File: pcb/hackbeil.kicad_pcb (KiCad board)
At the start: 2 copper layers, 138 x 114 mm, 98 parts

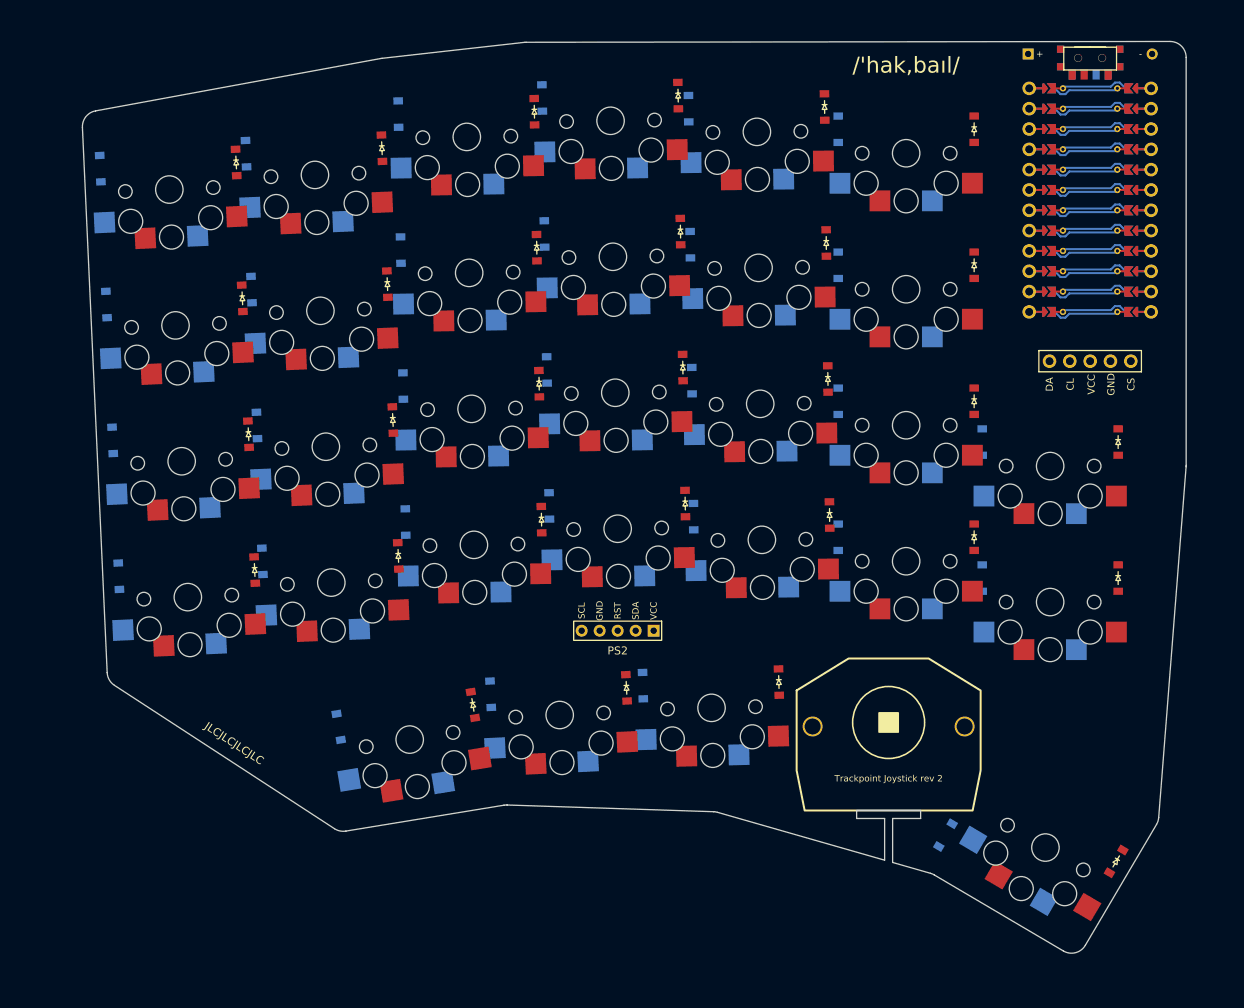
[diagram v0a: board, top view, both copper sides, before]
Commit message: Hand routed PCB
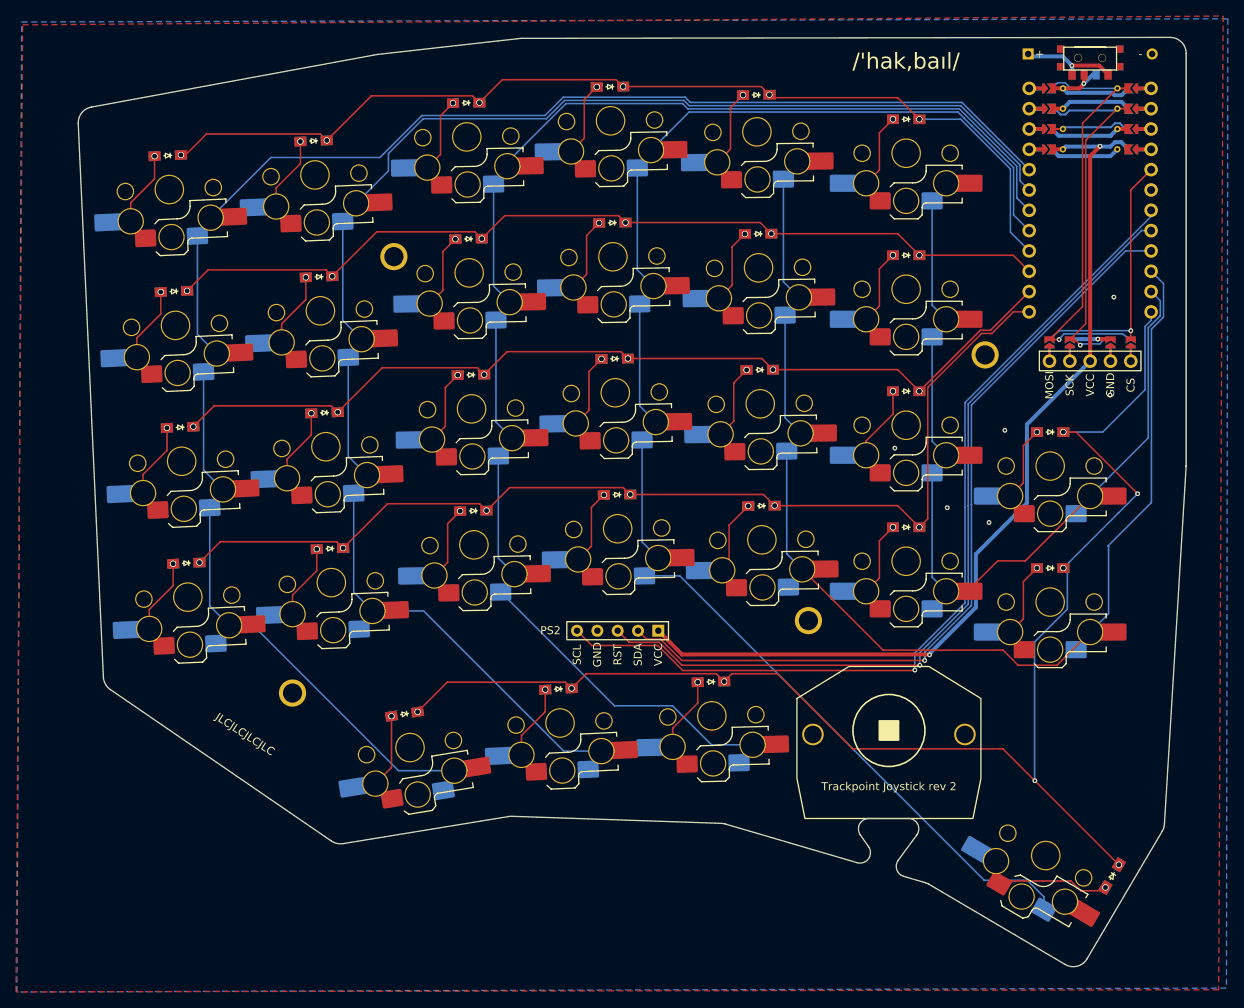
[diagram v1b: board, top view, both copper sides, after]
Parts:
- removed the ? at (219.8, 63.5)
- removed the ? at (135.8, 148.3)
- removed D31, D32, D33, D34, D35, D36, D37, D38, D39, D40, D41, D42, D43, D44, D45, D46, D47, D48, D49, D50, D51, D52, D53, D54, D55, D56, D57, D58, D59, D60: , lib:smd_diode
- added ?: , lib:text, F.Cu at (137.2, 147.1)
- added ?: , lib:text, F.Cu at (219.8, 63.0)
- added MH1: , ceoloide:mounting_hole_npth, F.Cu at (143.1, 142.0)
- added MH2: , ceoloide:mounting_hole_npth, F.Cu at (155.8, 87.4)
- added MH3: , ceoloide:mounting_hole_npth, F.Cu at (207.6, 132.9)
- added MH4: , ceoloide:mounting_hole_npth, F.Cu at (229.7, 99.7)
- S1, S10, S11, S12, S13, S14, S15, S16, S17, S18, S19, S2, S20, S21, S22, S23, S24, S25, S26, S27, S28, S29, S3, S30, S4, S5, S6, S7, S8, S9: footprint PG1350 -> ceoloide:switch_choc_v1_v2; moved to B.Cu
- moved D20 8.68 mm to (201.1, 67.2), turned to -179.3 degrees
- moved D27 8.63 mm to (157.1, 144.6), turned to -170.7 degrees
- moved D1 8.59 mm to (129.8, 125.8), turned to -177.4 degrees
- moved D5 8.59 mm to (147.8, 123.9), turned to -177.7 degrees
- moved D16 8.59 mm to (182.8, 66.2), turned to -179 degrees
- moved D7 8.59 mm to (146.4, 90.0), turned to -177.7 degrees
- moved D21 8.59 mm to (219.8, 121.3), turned to 180 degrees
- moved D22 8.59 mm to (219.8, 104.3), turned to 180 degrees
- moved D23 8.59 mm to (219.8, 87.3), turned to 180 degrees
- moved D24 8.59 mm to (219.8, 70.3), turned to 180 degrees
- moved D15 8.59 mm to (183.1, 83.2), turned to -179 degrees
- moved D25 8.59 mm to (237.8, 126.4), turned to 180 degrees
- moved D26 8.59 mm to (237.8, 109.4), turned to 180 degrees
- moved D14 8.59 mm to (183.4, 100.2), turned to -179 degrees
- moved D17 8.59 mm to (201.7, 118.6), turned to -179.3 degrees
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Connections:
- ? pad 2: P08 -> TP_SDA
- ? pad 3: P08 -> TP_RST
- ? pad 5: P06 -> TP_SCL
- DISP1 pad 1: P10 -> DISP1_1
- DISP1 pad 2: GND -> VCC
- DISP1 pad 3: VCC -> DISP1_3
- DISP1 pad 4: P3 -> DISP1_4
- DISP1 pad 5: P2 -> DISP1_0
- MCU1 pad 10: MCU1_10 -> COL4
- MCU1 pad 101: P1 -> NV_MOSI
- MCU1 pad 102: P0 -> NV_SCK
- MCU1 pad 11: MCU1_11 -> COL5
- MCU1 pad 12: MCU1_12 -> ROW4
- MCU1 pad 13: MCU1_13 -> ROW3
- MCU1 pad 14: MCU1_14 -> ROW2
- MCU1 pad 15: MCU1_15 -> ROW1
- MCU1 pad 16: MCU1_16 -> ROW0
- MCU1 pad 17: MCU1_17 -> COL3
- MCU1 pad 18: MCU1_18 -> COL2
- MCU1 pad 19: MCU1_19 -> COL1
- MCU1 pad 20: MCU1_20 -> COL0
- MCU1 pad 5: MCU1_5 -> NV_CS
- MCU1 pad 6: MCU1_6 -> (no net)
- MCU1 pad 7: MCU1_7 -> TP_SCL
- MCU1 pad 8: MCU1_8 -> TP_RST
- MCU1 pad 9: MCU1_9 -> TP_SDA
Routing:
- net (no net): track 337.7 -> 0.00 mm
- net COL0: track 0.00 -> 196.6 mm
- net ROW4: track 0.00 -> 179.6 mm, vias 0 -> 8
- net COL1: track 0.00 -> 179.5 mm
- net COL3: track 0.00 -> 173.8 mm
- net COL2: track 0.00 -> 163.8 mm
- net COL4: track 0.00 -> 139.0 mm
- net ROW3: track 0.00 -> 131.8 mm, vias 0 -> 6
- net ROW0: track 0.00 -> 124.8 mm, vias 0 -> 6
- net VCC: track 0.00 -> 118.2 mm, vias 0 -> 2
- net ROW2: track 0.00 -> 117.0 mm, vias 0 -> 6
- net TP_SCL: track 0.00 -> 114.0 mm, vias 0 -> 1
- net ROW1: track 0.00 -> 113.4 mm, vias 0 -> 6
- net TP_RST: track 0.00 -> 106.6 mm, vias 0 -> 1
- net TP_SDA: track 0.00 -> 102.2 mm, vias 0 -> 1
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- added copper zone on B.Cu, net GND
- added copper zone on F.Cu, net GND
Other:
- board size 138 x 114 mm -> 138.5 x 116.2 mm

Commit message: Add teardrops and smooth traces
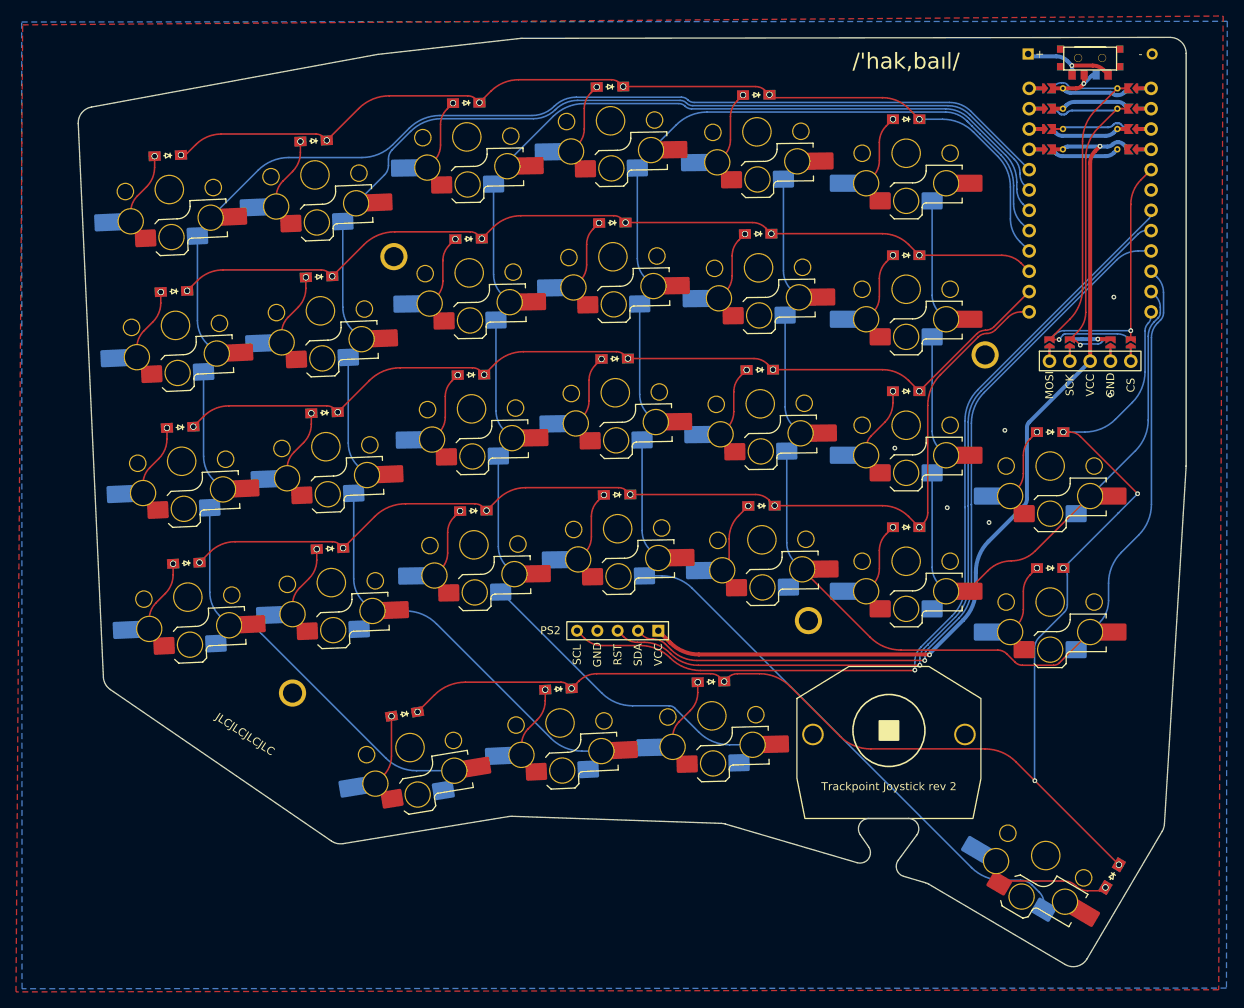
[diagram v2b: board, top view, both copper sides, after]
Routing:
- net COL0: track 196.6 -> 193.1 mm
- net COL1: track 179.5 -> 176.9 mm
- net COL2: track 163.8 -> 161.3 mm
- net ROW4: track 179.6 -> 177.3 mm
- net COL3: track 173.8 -> 171.7 mm
- net COL4: track 139.0 -> 137.0 mm
- net ROW0: track 124.8 -> 122.8 mm
- net ROW3: track 131.8 -> 129.9 mm
- net ROW1: track 113.4 -> 112.0 mm
- net ROW2: track 117.0 -> 115.6 mm
- net TP_SCL: track 114.0 -> 112.7 mm
- net COL5: track 96.5 -> 95.2 mm
- net VCC: track 118.2 -> 116.9 mm
- net TP_RST: track 106.6 -> 105.5 mm
- net TP_SDA: track 102.2 -> 101.0 mm
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
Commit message: Traced by combination of freerouting and manual routing
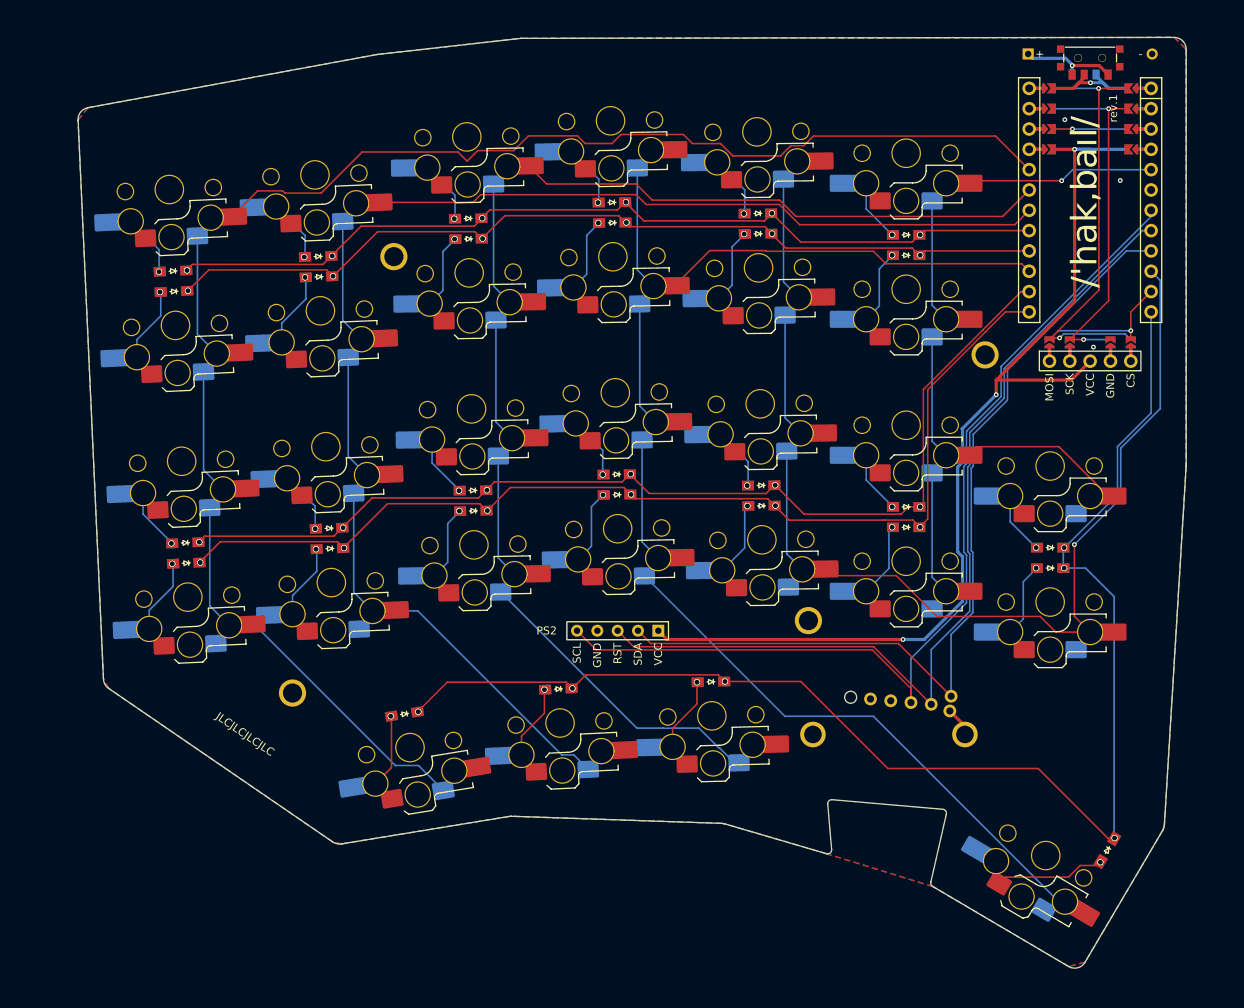
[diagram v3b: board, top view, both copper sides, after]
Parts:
- removed ?: , lib:trackpoint_header
- removed ?: , lib:niceview_headers
- removed ? (x2): , lib:text
- removed ?: , lib:trackpoint_joystick
- added BAT1: , hackbeil:battery, F.Cu at (242.8, 62.1)
- added RotaryEncoder_EVQWGD0011: RollerEncoder_EVQWGD001, hackbeil:RotaryEncoder_EVQWGD001, F.Cu at (218.6, 148.7)
- added TPH1: , hackbeil:trackpoint_header, F.Cu at (183.7, 134.2)
- added TPJ1: , hackbeil:trackpad_joystick_mounting_holes, B.Cu at (217.6, 146.7)
- D1, D10, D11, D12, D13, D14, D15, D16, D17, D18, D19, D2, D20, D21, D22, D23, D24, D25, D26, D27, D28, D29, D3, D30, D4, D5, D6, D7, D8, D9: footprint lib:smd_diode -> hackbeil:diode
- DISP1: footprint ceoloide:display_nice_view -> hackbeil:nice_view
- MCU1: footprint ceoloide:mcu_nice_nano -> hackbeil:mcu_nice_nano
- MH1, MH2, MH3, MH4: footprint ceoloide:mounting_hole_npth -> hackbeil:mounting_hole
- S1, S10, S11, S12, S13, S14, S15, S16, S17, S18, S19, S2, S20, S21, S22, S23, S24, S25, S26, S27, S28, S29, S3, S30, S4, S5, S6, S7, S8, S9: footprint ceoloide:switch_choc_v1_v2 -> hackbeil:switch_choc_v1_v2
- moved D16 67.5 mm to (147.8, 123.9), turned to -177.7 degrees
- moved D11 64.1 mm to (219.8, 118.7), turned to 180 degrees
- moved D17 62.3 mm to (146.4, 90.0), turned to -177.7 degrees
- moved D14 59.3 mm to (129.8, 125.8), turned to -177.4 degrees
- moved D12 57.4 mm to (219.8, 84.7), turned to 180 degrees
- moved D15 55.5 mm to (128.3, 91.8), turned to -177.4 degrees
- moved D13 54.5 mm to (237.8, 123.8), turned to 180 degrees
- moved D20 52.9 mm to (183.7, 117.2), turned to -179 degrees
- moved D21 52.9 mm to (183.1, 83.2), turned to -179 degrees
- moved D24 51.0 mm to (219.8, 121.3)
- moved D7 44.7 mm to (183.6, 114.7), turned to -179 degrees
- moved D25 43.0 mm to (219.8, 87.3)
- moved D10 41.2 mm to (201.3, 82.0), turned to -179.3 degrees
- moved D18 39.9 mm to (165.7, 119.2), turned to -179 degrees
- moved D8 38.1 mm to (183.0, 80.7), turned to -179 degrees
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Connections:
- D1 pad 1: ROW3 -> ROW2
- D1 pad 2: outer_bottom -> outer_home
- D1 pad 3: ROW3 -> ROW2
- D1 pad 4: outer_bottom -> outer_home
- D10 pad 1: ROW2 -> ROW0
- D10 pad 2: ring_home -> index_number
- D10 pad 3: ROW2 -> ROW0
- D10 pad 4: ring_home -> index_number
- D11 pad 1: ROW1 -> ROW2
- D11 pad 2: ring_top -> inner_home
- D11 pad 3: ROW1 -> ROW2
- D11 pad 4: ring_top -> inner_home
- D12 pad 2: ring_number -> inner_number
- D12 pad 4: ring_number -> inner_number
- D13 pad 1: ROW3 -> ROW4
- D13 pad 2: middle_bottom -> innest_home
- D13 pad 3: ROW3 -> ROW4
- D13 pad 4: middle_bottom -> innest_home
- D14 pad 1: ROW2 -> ROW3
- D14 pad 2: middle_home -> outer_bottom
- D14 pad 3: ROW2 -> ROW3
- D14 pad 4: middle_home -> outer_bottom
- D15 pad 2: middle_top -> outer_top
- D15 pad 4: middle_top -> outer_top
- D16 pad 1: ROW0 -> ROW3
- D16 pad 2: middle_number -> pinky_bottom
- D16 pad 3: ROW0 -> ROW3
- D16 pad 4: middle_number -> pinky_bottom
- D17 pad 1: ROW3 -> ROW1
- D17 pad 2: index_bottom -> pinky_top
- D17 pad 3: ROW3 -> ROW1
- D17 pad 4: index_bottom -> pinky_top
- D18 pad 1: ROW2 -> ROW3
- D18 pad 2: index_home -> ring_bottom
- D18 pad 3: ROW2 -> ROW3
- D18 pad 4: index_home -> ring_bottom
- D19 pad 2: index_top -> ring_top
- D19 pad 4: index_top -> ring_top
- D2 pad 1: ROW2 -> ROW0
- D2 pad 2: outer_home -> outer_number
- D2 pad 3: ROW2 -> ROW0
- D2 pad 4: outer_home -> outer_number
- D20 pad 1: ROW0 -> ROW3
- D20 pad 2: index_number -> middle_bottom
- D20 pad 3: ROW0 -> ROW3
- D20 pad 4: index_number -> middle_bottom
- D21 pad 1: ROW3 -> ROW1
- D21 pad 2: inner_bottom -> middle_top
- D21 pad 3: ROW3 -> ROW1
- D21 pad 4: inner_bottom -> middle_top
- D22 pad 1: ROW2 -> ROW3
- D22 pad 2: inner_home -> index_bottom
- D22 pad 3: ROW2 -> ROW3
- D22 pad 4: inner_home -> index_bottom
- D23 pad 2: inner_top -> index_top
- D23 pad 4: inner_top -> index_top
- D24 pad 1: ROW0 -> ROW3
- D24 pad 2: inner_number -> inner_bottom
- D24 pad 3: ROW0 -> ROW3
- D24 pad 4: inner_number -> inner_bottom
- D25 pad 1: ROW4 -> ROW1
- D25 pad 2: innest_bottom -> inner_top
- D25 pad 3: ROW4 -> ROW1
- D25 pad 4: innest_bottom -> inner_top
- D26 pad 2: innest_home -> innest_bottom
- D26 pad 4: innest_home -> innest_bottom
- D3 pad 1: ROW1 -> ROW2
- D3 pad 2: outer_top -> pinky_home
- D3 pad 3: ROW1 -> ROW2
- D3 pad 4: outer_top -> pinky_home
- D4 pad 2: outer_number -> pinky_number
- D4 pad 4: outer_number -> pinky_number
- D5 pad 1: ROW3 -> ROW2
- D5 pad 2: pinky_bottom -> ring_home
- D5 pad 3: ROW3 -> ROW2
- D5 pad 4: pinky_bottom -> ring_home
- D6 pad 1: ROW2 -> ROW0
- D6 pad 2: pinky_home -> ring_number
- D6 pad 3: ROW2 -> ROW0
- D6 pad 4: pinky_home -> ring_number
- D7 pad 1: ROW1 -> ROW2
- D7 pad 2: pinky_top -> middle_home
- D7 pad 3: ROW1 -> ROW2
- D7 pad 4: pinky_top -> middle_home
- D8 pad 2: pinky_number -> middle_number
- D8 pad 4: pinky_number -> middle_number
- D9 pad 1: ROW3 -> ROW2
- D9 pad 2: ring_bottom -> index_home
- D9 pad 3: ROW3 -> ROW2
- D9 pad 4: ring_bottom -> index_home
- MCU1 pad 11: COL5 -> NV_CS
- MCU1 pad 15: ROW1 -> COL3
- MCU1 pad 16: ROW0 -> ROW1
- MCU1 pad 17: COL3 -> ROW0
- MCU1 pad 18: COL2 -> COL1
- MCU1 pad 19: COL1 -> COL2
- MCU1 pad 5: NV_CS -> COL5
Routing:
- net GND: track 34.6 -> 3.72 mm, vias 7 -> 3
- net NV_CS: track 32.6 -> 17.7 mm
- net ROW2: track 115.6 -> 130.0 mm
- net VCC: track 116.9 -> 127.5 mm, vias 2 -> 3
- net COL1: track 176.9 -> 166.4 mm
- net ROW0: track 122.8 -> 112.4 mm
- net TP_SDA: track 101.0 -> 110.5 mm, vias 1 -> 0
- net COL2: track 161.3 -> 152.1 mm
- net TP_RST: track 105.5 -> 114.5 mm, vias 1 -> 0
- net COL3: track 171.7 -> 163.4 mm
- net TP_SCL: track 112.7 -> 120.7 mm, vias 1 -> 0
- net ROW4: track 177.3 -> 172.9 mm, vias 8 -> 6
- net COL5: track 95.2 -> 91.6 mm, vias 0 -> 1
- net COL4: track 137.0 -> 134.2 mm, vias 0 -> 1
- net ROW3: track 129.9 -> 131.9 mm
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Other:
- board size 138.5 x 116.2 mm -> 138.5 x 116.3 mm
- board text added: "/'hak,baıl/"
- board text added: "JLCJLCJLCJLC"
- board text added: "Trackpoint Joystick rev 2"
- board text added: "rev.1"
